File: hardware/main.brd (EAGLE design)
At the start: 49.2 x 49.5 mm, 16 parts, among them IC1 ATMEGA168-AU, J1 AVR_SPI_PRG_6NS

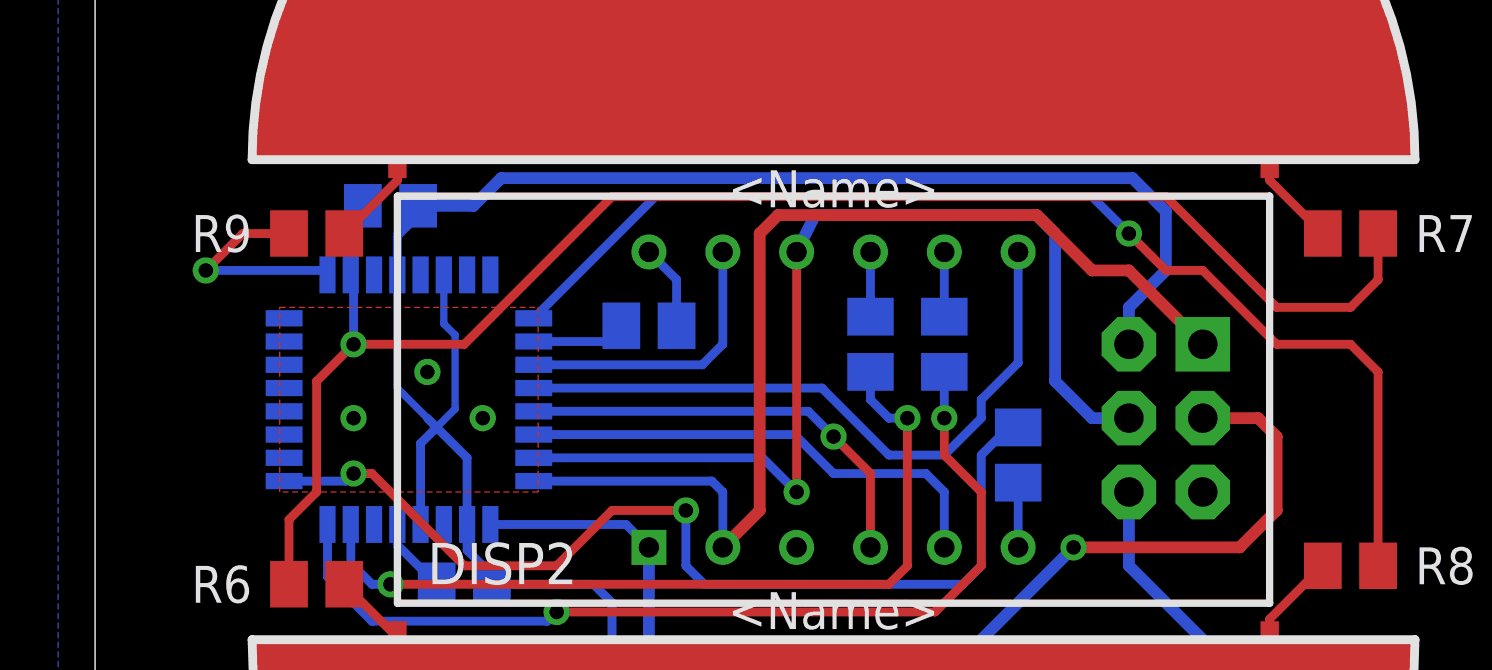
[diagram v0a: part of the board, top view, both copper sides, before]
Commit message: HARDWARE MISTAKE: Did not include connection to Reset line. This makes the AVR unprogrammable without a jumper wire. Fixed.
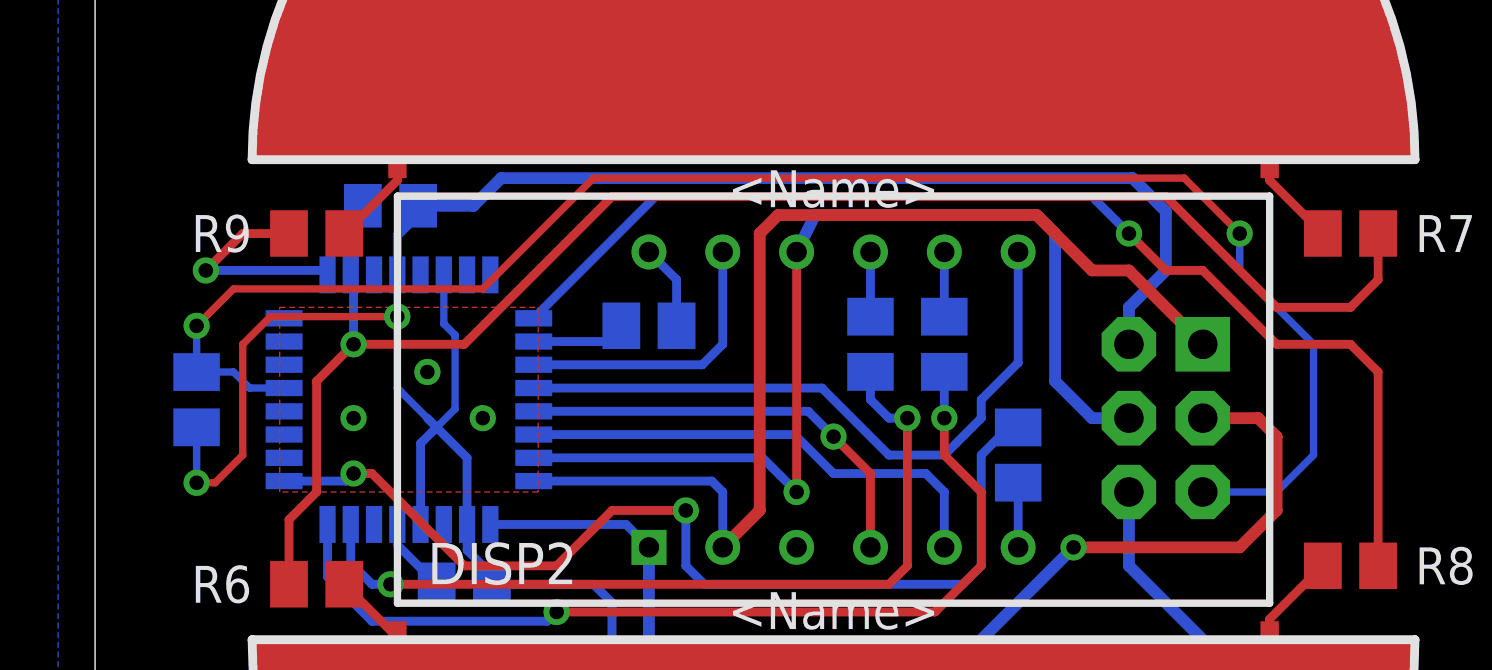
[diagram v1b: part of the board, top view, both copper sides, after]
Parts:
- added R5: 10K, rcl:M0805
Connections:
- new net RESET: IC1.29, J1.5, R5.2
- net VCC: now also R5.1
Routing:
- net RESET: track 0.00 -> 56.6 mm, vias 0 -> 2
- net VCC: track 73.7 -> 87.2 mm, vias 0 -> 2
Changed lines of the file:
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@@
 <attribute name="NAME" x="33.655" y="27.94" size="1.27" layer="26" ratio="10" rot="MR270"/>
+</element>
+<element name="R5" library="rcl" package="M0805" value="10K" x="3.4925" y="24.765" smashed="yes" rot="MR90">
+<attribute name="NAME" x="0.9525" y="23.495" size="1.27" layer="26" rot="MR90"/>
 </element>
 </elements>
@@
 <wire x1="12.795" y1="22.765" x2="11.7475" y2="23.8125" width="0.3048" layer="16"/>
 <wire x1="11.7475" y1="23.8125" x2="11.43" y2="24.13" width="0.3048" layer="16"/>
-<wire x1="11.43" y1="24.13" x2="10.395" y2="25.165" width="0.254" layer="16"/>
+<wire x1="11.43" y1="24.13" x2="10.4775" y2="25.0825" width="0.254" layer="16"/>
 <wire x1="11.195" y1="20.4724" x2="11.195" y2="23.26" width="0.3048" layer="16"/>
 <wire x1="11.195" y1="23.26" x2="11.7475" y2="23.8125" width="0.3048" layer="16"/>
-<wire x1="10.395" y1="29.0576" x2="10.395" y2="25.165" width="0.254" layer="16"/>
+<wire x1="10.395" y1="29.0576" x2="10.395" y2="27.6225" width="0.254" layer="16"/>
 <wire x1="10.395" y1="29.0576" x2="10.395" y2="30.3975" width="0.3048" layer="16"/>
 <wire x1="10.395" y1="30.3975" x2="11.11" y2="31.1125" width="0.3048" layer="16"/>
@@
 <wire x1="12.3825" y1="26.9875" x2="12.3825" y2="24.4475" width="0.254" layer="16"/>
 <wire x1="12.3825" y1="24.4475" x2="11.7475" y2="23.8125" width="0.254" layer="16"/>
+<contactref element="R5" pad="1"/>
+<wire x1="3.4925" y1="23.815" x2="3.4925" y2="21.9075" width="0.254" layer="16"/>
+<via x="3.4925" y="21.9075" extent="1-16" drill="0.5"/>
+<wire x1="3.4925" y1="21.9075" x2="4.1275" y2="21.9075" width="0.254" layer="1"/>
+<wire x1="4.1275" y1="21.9075" x2="5.08" y2="22.86" width="0.254" layer="1"/>
+<wire x1="5.08" y1="22.86" x2="5.08" y2="26.67" width="0.254" layer="1"/>
+<wire x1="5.08" y1="26.67" x2="6.0325" y2="27.6225" width="0.254" layer="1"/>
+<wire x1="6.0325" y1="27.6225" x2="10.395" y2="27.6225" width="0.254" layer="1"/>
+<via x="10.395" y="27.6225" extent="1-16" drill="0.5"/>
+<wire x1="10.395" y1="27.6225" x2="10.395" y2="25.165" width="0.254" layer="16"/>
+<wire x1="10.395" y1="25.165" x2="10.4775" y2="25.0825" width="0.254" layer="16"/>
 </signal>
 <signal name="GND">
@@
 <wire x1="7.995" y1="20.4724" x2="7.995" y2="18.675" width="0.3048" layer="16"/>
 </signal>
+<signal name="RESET">
+<contactref element="J1" pad="5"/>
+<contactref element="IC1" pad="29"/>
+<contactref element="R5" pad="2"/>
+<wire x1="6.5024" y1="25.165" x2="5.315" y2="25.165" width="0.254" layer="16"/>
+<wire x1="5.315" y1="25.165" x2="4.7625" y2="25.7175" width="0.254" layer="16"/>
+<wire x1="4.7625" y1="25.7175" x2="3.495" y2="25.7175" width="0.254" layer="16"/>
+<wire x1="3.495" y1="25.7175" x2="3.4925" y2="25.715" width="0.254" layer="16"/>
+<wire x1="38.1" y1="21.59" x2="40.64" y2="21.59" width="0.254" layer="16"/>
+<wire x1="40.64" y1="21.59" x2="41.91" y2="22.86" width="0.254" layer="16"/>
+<wire x1="41.91" y1="22.86" x2="41.91" y2="26.67" width="0.254" layer="16"/>
+<wire x1="41.91" y1="26.67" x2="39.37" y2="29.21" width="0.254" layer="16"/>
+<wire x1="39.37" y1="29.21" x2="39.37" y2="30.48" width="0.254" layer="16"/>
+<via x="39.37" y="30.48" extent="1-16" drill="0.5"/>
+<wire x1="39.37" y1="30.48" x2="37.465" y2="32.385" width="0.254" layer="1"/>
+<wire x1="37.465" y1="32.385" x2="17.145" y2="32.385" width="0.254" layer="1"/>
+<wire x1="17.145" y1="32.385" x2="13.335" y2="28.575" width="0.254" layer="1"/>
+<wire x1="13.335" y1="28.575" x2="4.7625" y2="28.575" width="0.254" layer="1"/>
+<wire x1="4.7625" y1="28.575" x2="3.4925" y2="27.305" width="0.254" layer="1"/>
+<via x="3.4925" y="27.305" extent="1-16" drill="0.5"/>
+<wire x1="3.4925" y1="27.305" x2="3.4925" y2="25.715" width="0.254" layer="16"/>
+</signal>
 </signals>

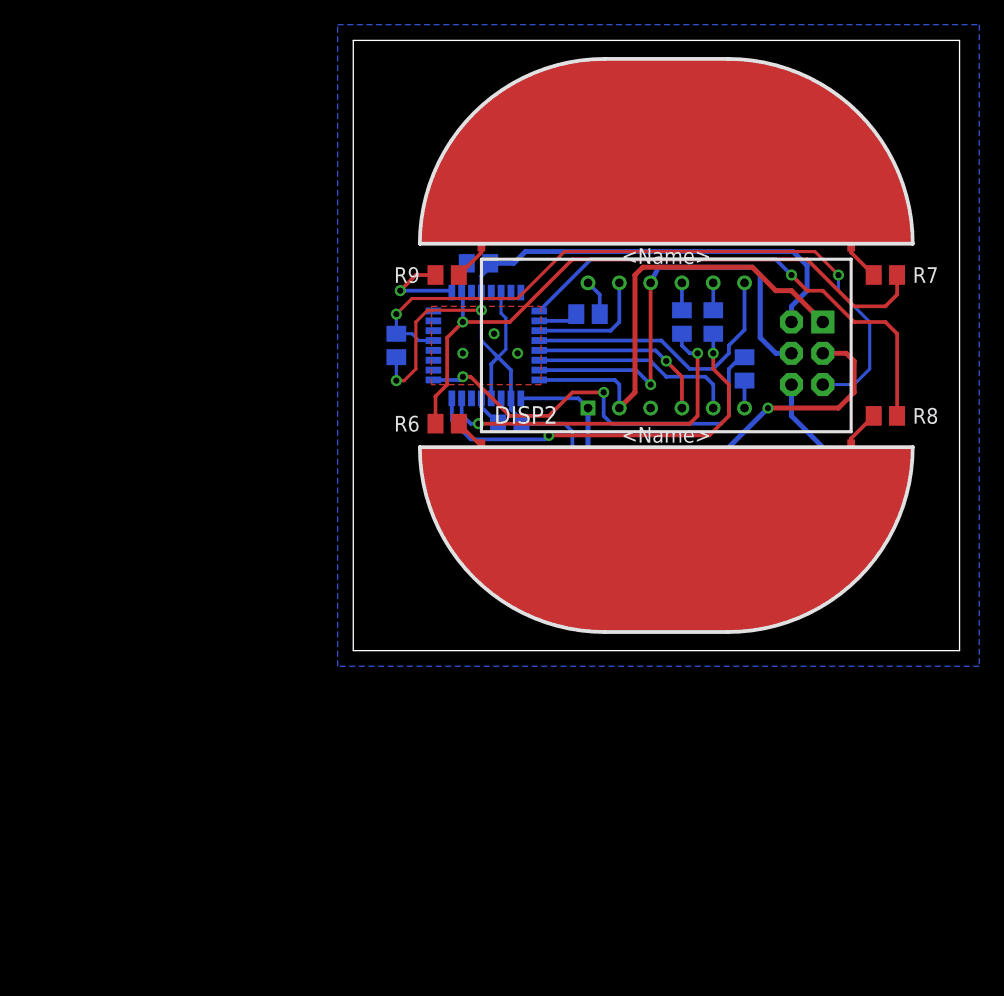
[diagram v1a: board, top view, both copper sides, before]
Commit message: Hardware updates: 1. Changed display connection for cleaner layout 2. Changed touch sensor configuration for CVD touch sensing, and simpler layout 3. Changed passives to 0603 to ensmallen the board 4. Ensmallened the board 5. Rounded them corners
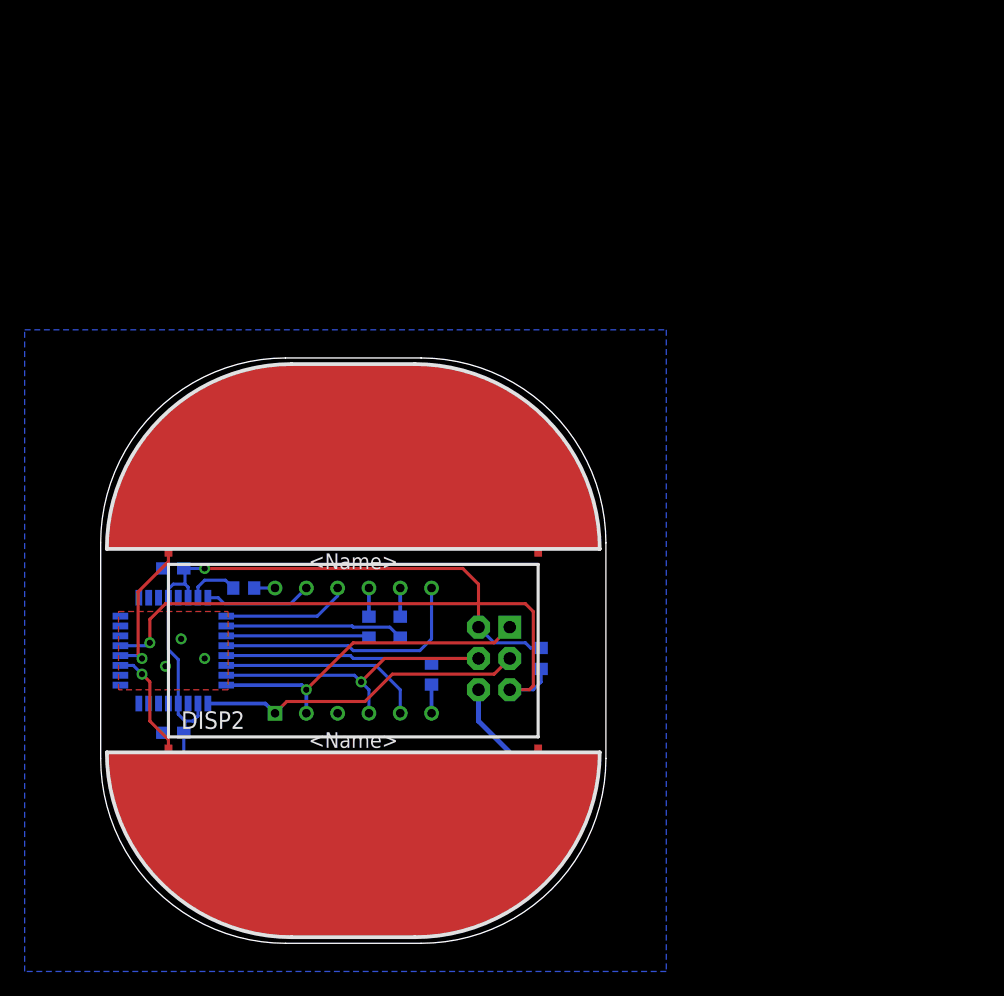
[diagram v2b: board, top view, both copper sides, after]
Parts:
- removed R6, R7, R8, R9: (no value), rcl:M0805
- C1, C2: device rcl:C0805 -> rcl:C0603
- R1, R2, R3, R4, R5: device rcl:M0805 -> rcl:R0603
- moved C2 37.1 mm to (-14.6, -6.67)
- moved R4 35.7 mm to (-8.89, 5.08)
- moved R2 35.5 mm to (3.81, 1.91)
- moved R3 35.5 mm to (1.27, 1.91)
- moved BATT1 35.5 mm to (0.00, -14.0)
- moved DISP2 35.5 mm to (0.00, 0.00)
- moved DOWN 35.5 mm to (0.00, -8.26)
- moved IC1 35.5 mm to (-14.6, 0.00)
- moved J1 35.5 mm to (11.4, -0.64)
- moved R1 35.5 mm to (6.35, -1.91)
- moved UP 35.5 mm to (0.00, 8.26)
- moved C1 35.0 mm to (-14.6, 6.67)
- moved R5 28.0 mm to (15.2, -0.64), turned to 270 degrees
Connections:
- removed net N$1: DOWN.SND, R6.1
- removed net N$6: DOWN.RCV, R8.1
- removed net N$7: R7.1, UP.SND
- removed net N$8: R9.1, UP.RCV
- removed net TCH_SND: IC1.2, R6.2, R7.2
- net 7S_A: now also IC1.8; no longer IC1.11
- net 7S_C: now also IC1.15, J1.4; no longer IC1.13
- net 7S_F: now also IC1.9; no longer IC1.15, J1.4
- net 7S_PW_1: now also IC1.13; no longer IC1.25
- net 7S_PW_10: now also IC1.10; no longer IC1.24
- net 7S_PW_100: now also IC1.11; no longer IC1.23
- net 7S_PW_1000: now also IC1.7; no longer IC1.10
- net TCH_RCV_DN: now also DOWN.SND, IC1.27; no longer IC1.9, R8.2
- net TCH_RCV_UP: now also IC1.28, UP.RCV; no longer IC1.1, R9.2
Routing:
- net TCH_SND: track 52.5 -> 0.00 mm, vias 1 -> 0
- net TCH_RCV_DN: track 39.9 -> 9.28 mm
- net VCC: track 87.2 -> 60.2 mm, vias 2 -> 1
- net 7S_F: track 35.9 -> 10.4 mm, vias 1 -> 0
- net 7S_PW_10: track 32.9 -> 14.5 mm, vias 2 -> 0
- net 7S_PW_1: track 34.1 -> 16.9 mm, vias 2 -> 0
- net 7S_PW_100: track 28.6 -> 11.6 mm, vias 2 -> 0
- net 7S_E: track 38.8 -> 26.7 mm, vias 1 -> 0
- net 7S_D: track 37.2 -> 27.2 mm, vias 0 -> 1
- net 7S_C: track 15.0 -> 24.3 mm
- net RESET: track 56.6 -> 48.2 mm, vias 2 -> 1
- net TCH_RCV_UP: track 7.63 -> 11.9 mm
- net N$8: track 3.30 -> 0.00 mm
- net N$7: track 3.30 -> 0.00 mm
- net N$6: track 3.30 -> 0.00 mm
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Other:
- board size 49.2 x 49.5 mm -> 41 x 47.5 mm

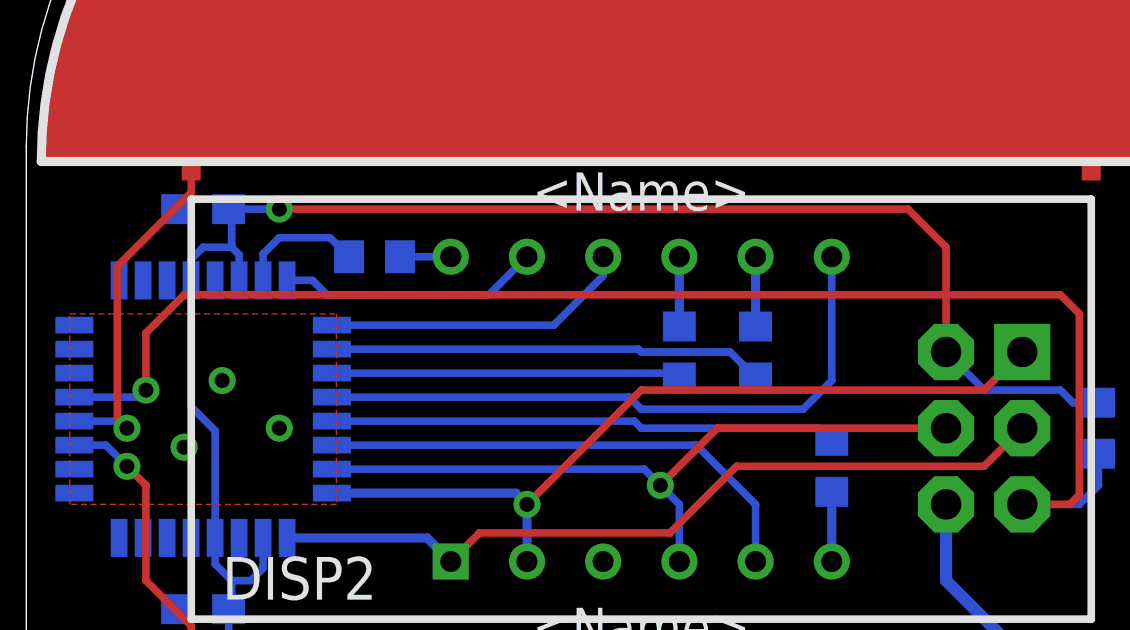
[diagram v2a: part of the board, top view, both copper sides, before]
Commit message: Fixed error in schematic preventing back-annotation Fixed crossing traces in PCB Updated manufacturing data
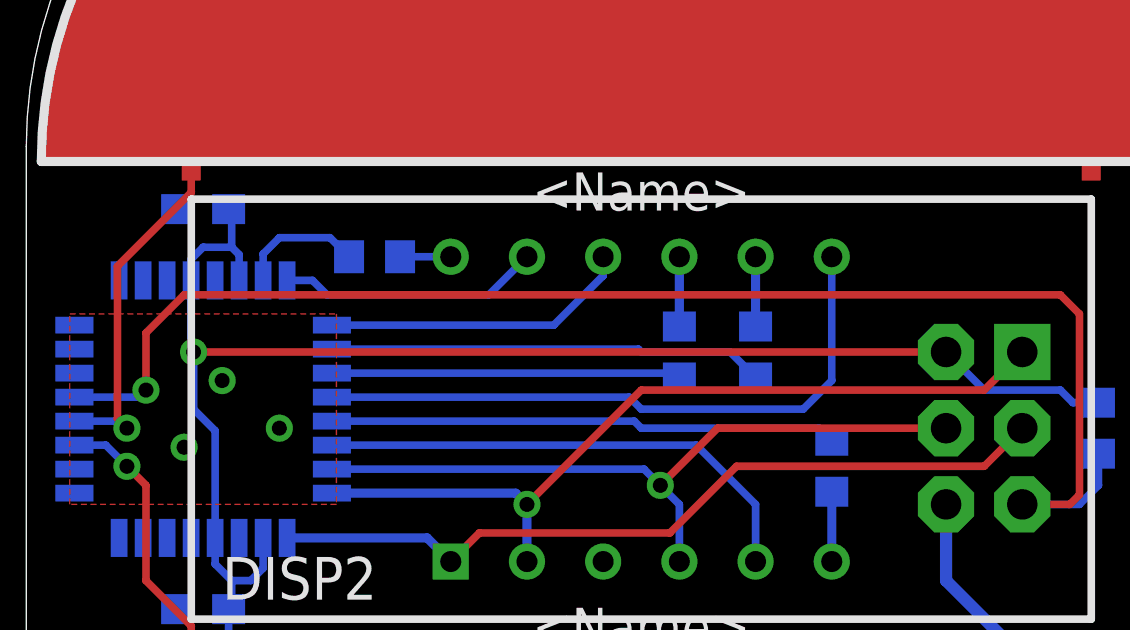
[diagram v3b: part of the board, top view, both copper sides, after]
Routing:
- net VCC: track 60.2 -> 57.4 mm
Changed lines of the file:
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@@
 <setting verticaltext="up"/>
 </settings>
-<grid distance="0.05" unitdist="inch" unit="mm" style="lines" multiple="1" display="yes" altdistance="0.0125" altunitdist="inch" altunit="inch"/>
+<grid distance="0.05" unitdist="inch" unit="inch" style="lines" multiple="1" display="yes" altdistance="0.0125" altunitdist="inch" altunit="inch"/>
 <layers>
 <layer number="1" name="Top" color="4" fill="1" visible="yes" active="yes"/>
@@
 <param name="mdViaViaSameLayer" value="8mil"/>
 <param name="mnLayersViaInSmd" value="2"/>
-<param name="mdCopperDimension" value="20mil"/>
+<param name="mdCopperDimension" value="10mil"/>
 <param name="mdDrill" value="8mil"/>
 <param name="mdSmdStop" value="0mil"/>
@@
 <contactref element="R5" pad="1"/>
 <wire x1="-14.205" y1="-4.2926" x2="-14.205" y2="-0.7175" width="0.254" layer="16"/>
-<wire x1="-14.205" y1="-0.7175" x2="-15.005" y2="0.0825" width="0.254" layer="16"/>
-<wire x1="-15.005" y1="4.2926" x2="-15.005" y2="0.0825" width="0.254" layer="16"/>
 <wire x1="-15.005" y1="4.2926" x2="-15.005" y2="4.9975" width="0.254" layer="16"/>
 <wire x1="-15.005" y1="4.9975" x2="-14.605" y2="5.3975" width="0.254" layer="16"/>
@@
 <wire x1="13.97" y1="0.635" x2="11.43" y2="0.635" width="0.254" layer="16"/>
 <wire x1="11.43" y1="0.635" x2="10.16" y2="1.905" width="0.254" layer="16"/>
-<wire x1="10.16" y1="1.905" x2="10.16" y2="5.3975" width="0.254" layer="1"/>
-<wire x1="10.16" y1="5.3975" x2="8.89" y2="6.6675" width="0.254" layer="1"/>
-<wire x1="8.89" y1="6.6675" x2="-12.065" y2="6.6675" width="0.254" layer="1"/>
-<via x="-12.065" y="6.6675" extent="1-16" drill="0.5"/>
-<wire x1="-12.065" y1="6.6675" x2="-13.755" y2="6.6675" width="0.254" layer="16"/>
+<wire x1="10.16" y1="1.905" x2="-14.9225" y2="1.905" width="0.254" layer="1"/>
+<wire x1="-14.9225" y1="1.905" x2="-15.005" y2="1.905" width="0.254" layer="1"/>
+<via x="-14.9225" y="1.905" extent="1-16" drill="0.5"/>
+<wire x1="-15.005" y1="4.2926" x2="-15.005" y2="1.9875" width="0.254" layer="16"/>
+<wire x1="-15.005" y1="1.9875" x2="-14.9225" y2="1.905" width="0.254" layer="16"/>
+<wire x1="-14.9225" y1="1.905" x2="-14.9225" y2="0" width="0.254" layer="16"/>
+<wire x1="-14.9225" y1="0" x2="-14.205" y2="-0.7175" width="0.254" layer="16"/>
 </signal>
 <signal name="GND">
